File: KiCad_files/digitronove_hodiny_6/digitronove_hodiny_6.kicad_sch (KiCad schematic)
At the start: 54 parts, among them J1 Nixie_CATHODES, J2 Nixie_ANODES, J3 Conn_01x05, J4 Conn_01x05, J5 Conn_01x02, Q1 MPSA42, Q10 MPSA42, Q2 MPSA42, Q3 MPSA42, Q4 MPSA42, Q5 MPSA42, Q6 MPSA42, Q7 MPSA42, Q8 MPSA42, Q9 MPSA42, U1 WeMos_D1_mini, U10 74HC595, U12 AMS1117-3.3, U2 74HC595, U3 74HC595, U4 TLP627, U5 TLP627, U6 TLP627, U7 TLP627, U8 TLP627, U9 TLP627

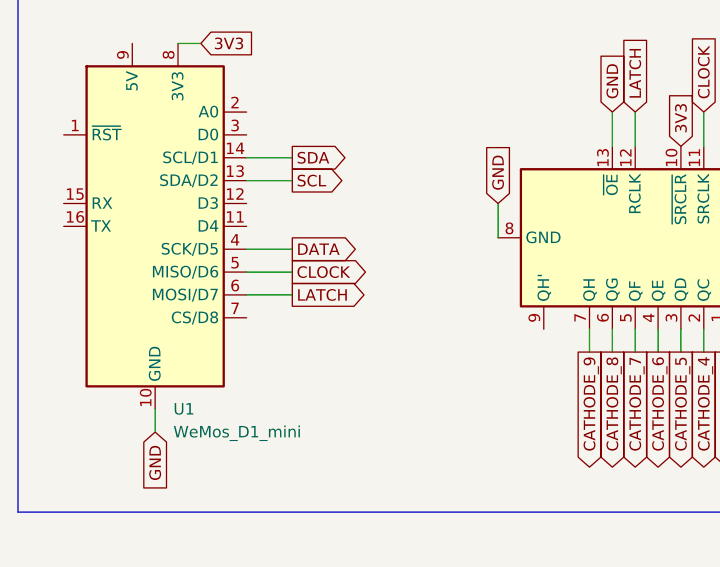
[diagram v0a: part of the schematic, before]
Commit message: KiCad PCB and Schema desing update
Nearly finished PCB desing. Changed the schema according to my breadboard prototype.
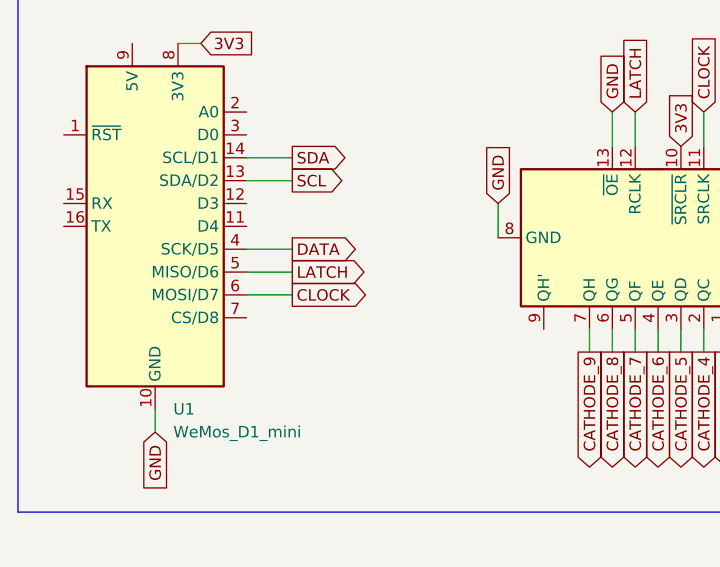
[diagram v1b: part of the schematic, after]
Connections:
- net CLOCK: now also U1.6 (MOSI/D7); no longer U1.5 (MISO/D6)
- net LATCH: now also U1.5 (MISO/D6); no longer U1.6 (MOSI/D7)

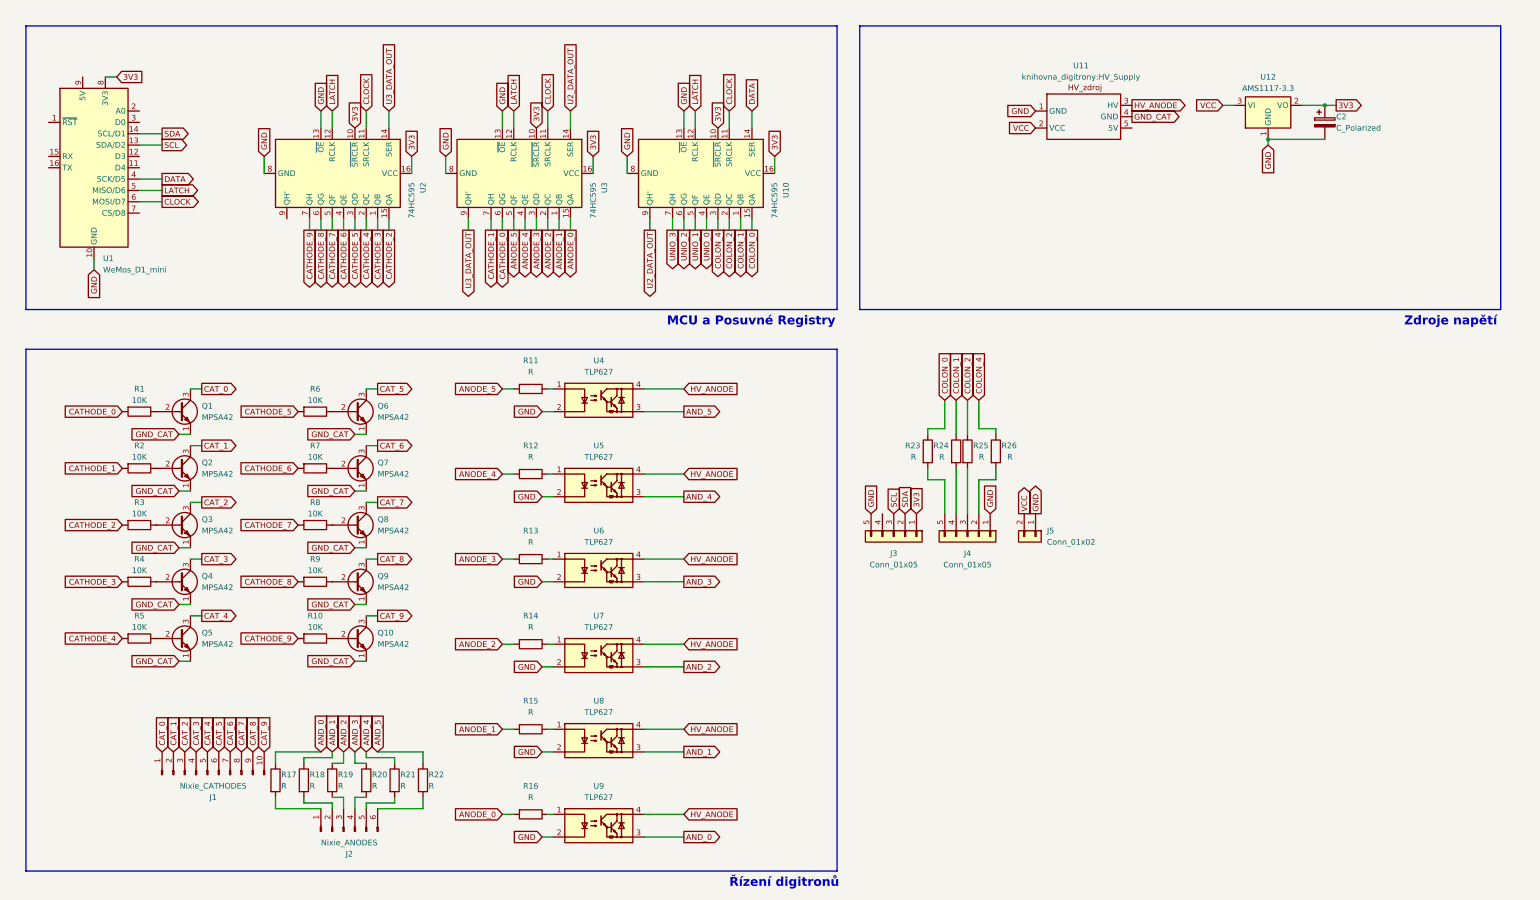
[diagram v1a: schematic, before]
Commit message: Created resources directory, EDA files update.
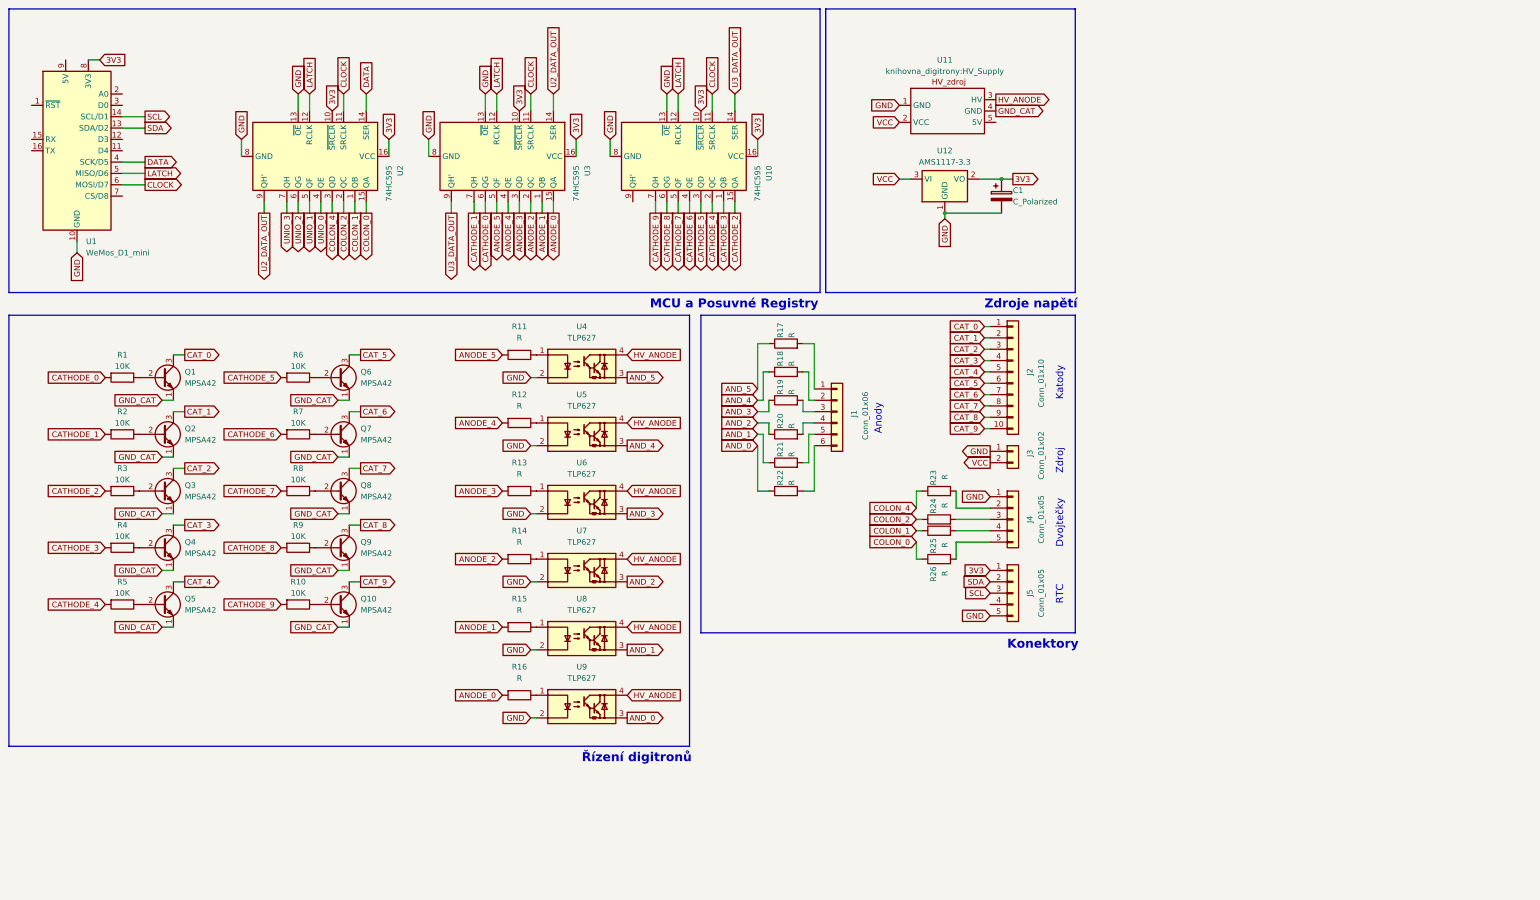
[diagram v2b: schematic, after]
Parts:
- J1: renamed from J2; value Nixie_ANODES -> Conn_01x06; symbol Connector:Conn_01x06_Pin -> Connector_Generic:Conn_01x06
- J2: renamed from J1; value Nixie_CATHODES -> Conn_01x10; symbol Connector:Conn_01x10_Pin -> Connector_Generic:Conn_01x10
- Q1, Q10, Q2, Q3, Q4, Q5, Q6, Q7, Q8, Q9: footprint Package_TO_SOT_THT:TO-92_Inline -> Package_TO_SOT_THT:TO-92_Inline_Wide
- renumbered C2 to C1, J5 to J3, J3 to J5, R22 to R17, R21 to R18, R20 to R19, R19 to R20, R18 to R21, R17 to R22, R26 to R23, R25 to R24, R24 to R25, R23 to R26, U2 to U10, U10 to U2
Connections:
- net SCL: now also U1.14 (SCL/D1); no longer U1.13 (SDA/D2)
- net SDA: now also U1.13 (SDA/D2); no longer U1.14 (SCL/D1)
- net at R17.2: now also J1.1 (Pin_1); no longer J1.6 (Pin_6)
- net at R18.2: now also J1.2 (Pin_2); no longer J1.5 (Pin_5)
- net at R21.2: now also J1.5 (Pin_5); no longer J1.2 (Pin_2)
- net at R22.2: now also J1.6 (Pin_6); no longer J1.1 (Pin_1)
- net at J1.3 (Pin_3): now also R19.2; no longer R20.2
- net at J1.4 (Pin_4): now also R20.2; no longer R19.2
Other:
- note added: "Anody"
- note added: "Dvojtečky"
- note added: "Katody"
- note added: "Konektory"
- note added: "RTC"
- note added: "Zdroj"
- title: (none) -> Digitronové Hodiny s ESP8266
- moved on the sheet: C1, J3, J4, J5, Q1, Q10, Q2, Q3, Q4, Q5, Q6, Q7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

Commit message: PCB Design update
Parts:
- added C2: C_Polarized, Capacitor_THT:CP_Radial_Tantal_D5.5mm_P2.50mm, symbol Device:C_Polarized
- renumbered U7 to U10, U8 to U11, U9 to U12, U10 to U4, U12 to U5, U11 to U6, U4 to U7, U5 to U8, U6 to U9
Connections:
- net GND: now also C2.2
- net SCL: now also U1.13 (SDA/D2); no longer U1.14 (SCL/D1)
- net SDA: now also U1.14 (SCL/D1); no longer U1.13 (SDA/D2)
- net VCC: now also C2.1
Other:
- moved on the sheet: C1, U5, U6
